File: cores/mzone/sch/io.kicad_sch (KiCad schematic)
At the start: 87 parts

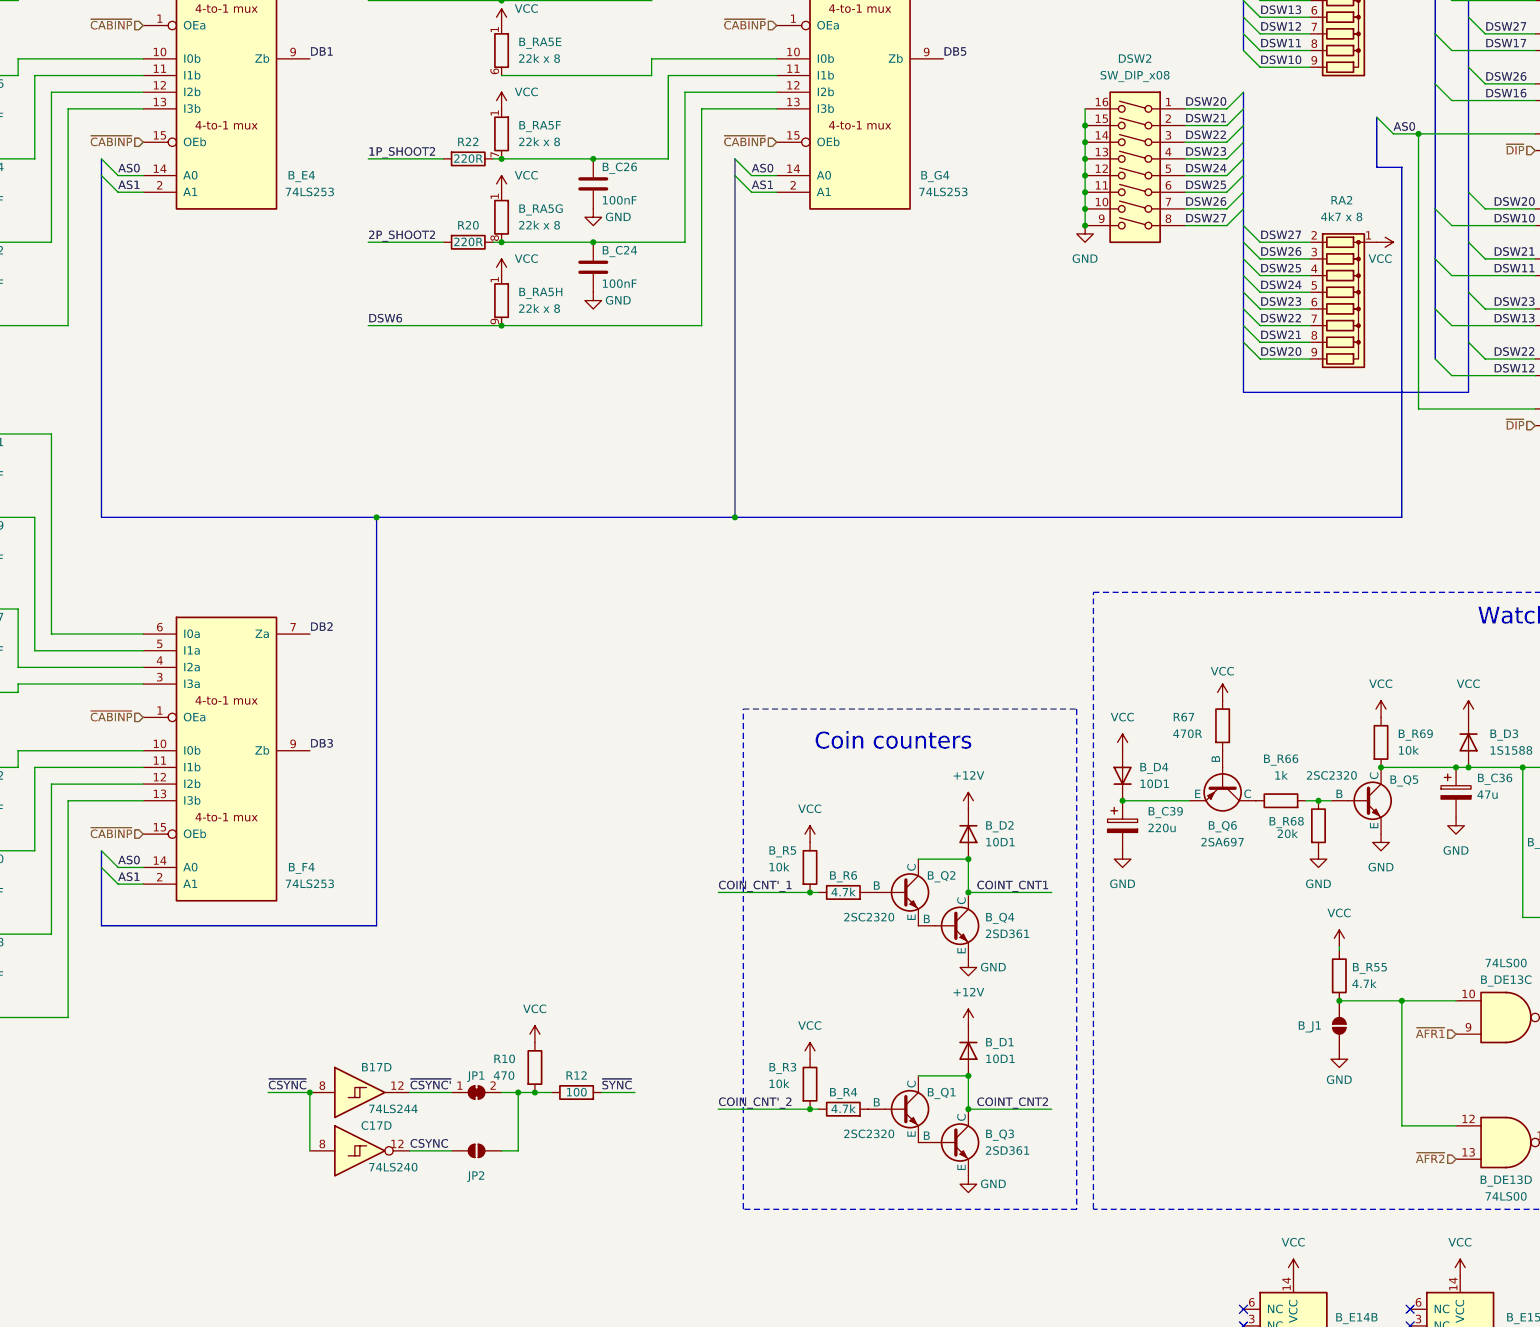
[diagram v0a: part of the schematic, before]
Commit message: mzone core
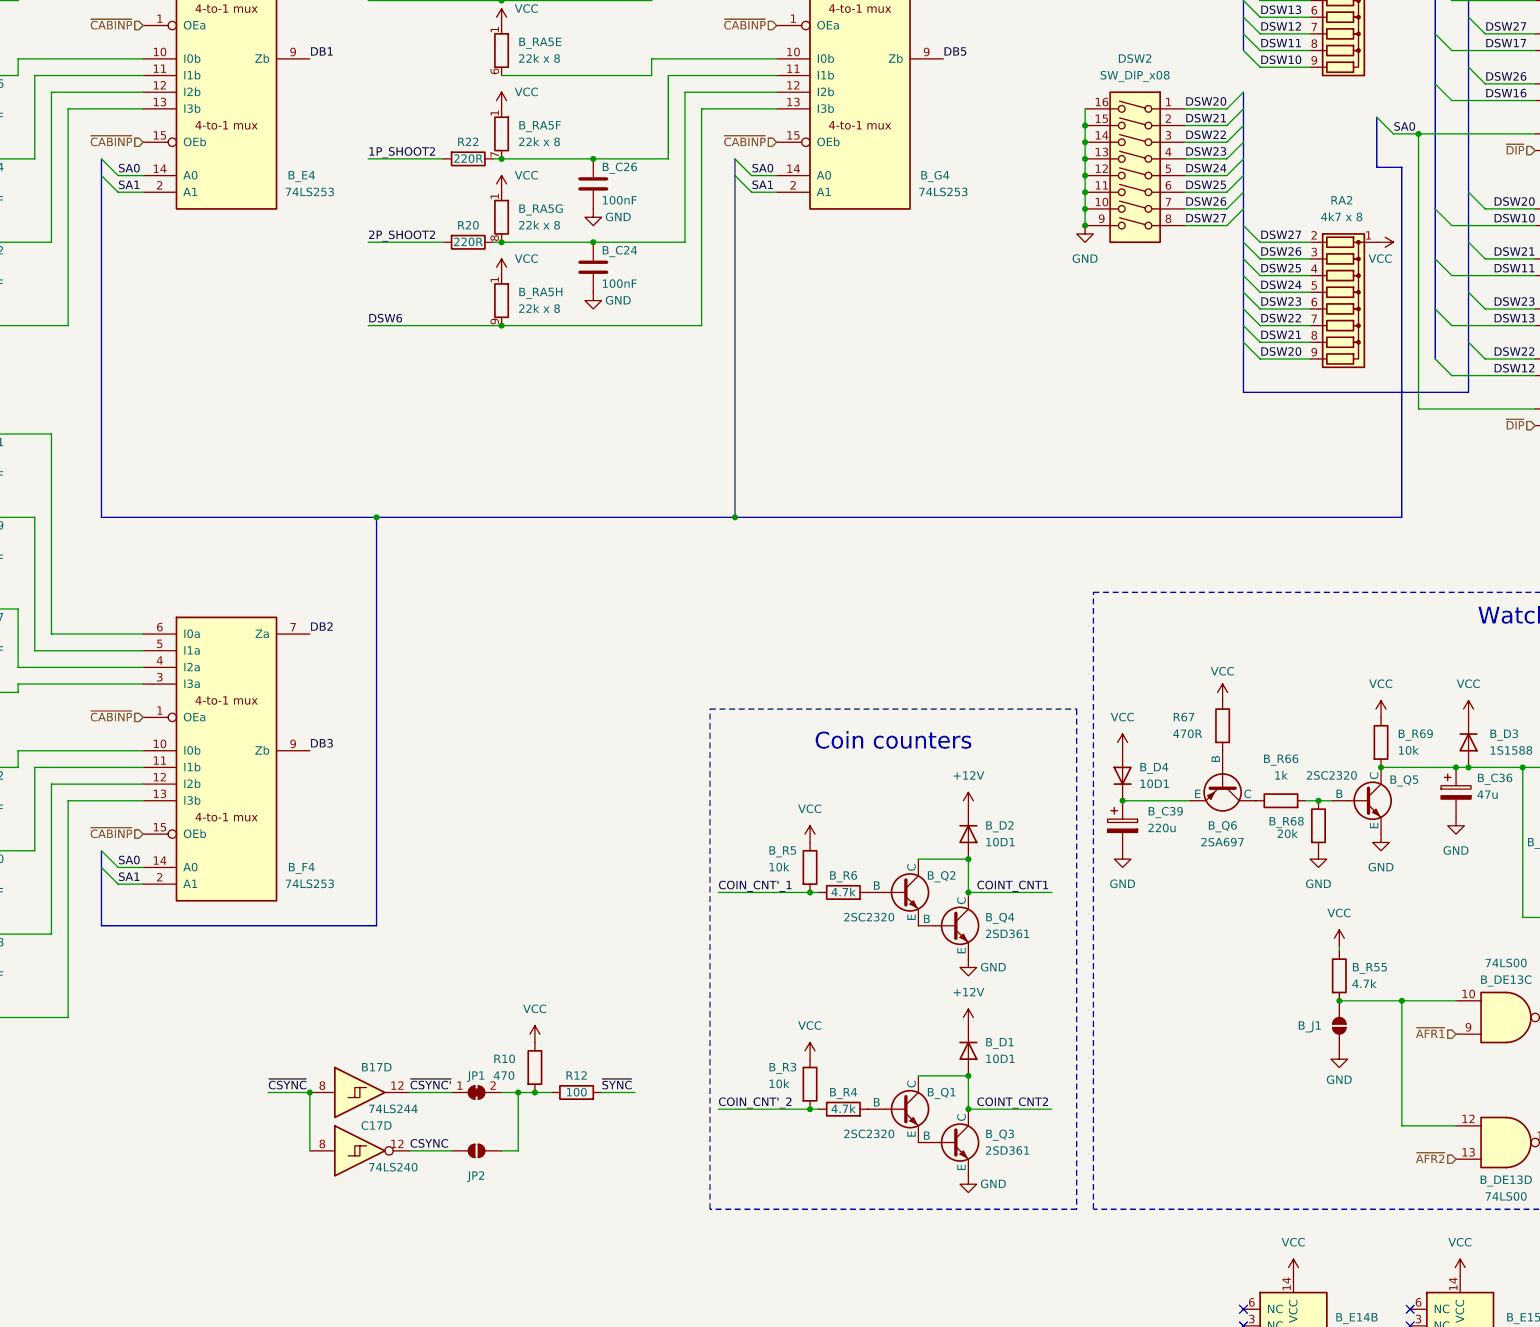
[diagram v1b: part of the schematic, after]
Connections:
- net AS0 renamed SA0
- net AS1 renamed SA1
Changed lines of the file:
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@@
 	)
 	(rectangle
-		(start 172.72 173.99)
+		(start 167.64 173.99)
 		(end 223.52 250.19)
 		(stroke
@@
 		)
 	)
-	(label "AS0"
+	(label "SA0"
 		(at 77.47 92.71 0)
 		(effects
@@
 		)
 	)
-	(label "AS0"
+	(label "SA0"
 		(at 271.78 86.36 0)
 		(effects
@@
 		)
 	)
-	(label "AS1"
+	(label "SA1"
 		(at 77.47 95.25 0)
 		(effects
@@
 		)
 	)
-	(label "AS1"
+	(label "SA1"
 		(at 173.99 95.25 0)
 		(effects
@@
 		)
 	)
-	(label "AS0"
+	(label "SA0"
 		(at 173.99 92.71 0)
 		(effects
@@
 		)
 	)
-	(label "AS0"
+	(label "SA0"
 		(at 77.47 198.12 0)
 		(effects
@@
 		)
 	)
-	(label "AS1"
+	(label "SA1"
 		(at 77.47 200.66 0)
 		(effects

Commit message: mzone core
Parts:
- added SW3: SW_DIP_x06, symbol Switch:SW_DIP_x06
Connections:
- net +12V: now also U?.B1 (+12V)
- net 1P_DOWN: now also U?.A11 (1P_DOWN)
- net 1P_RIGHT: now also U?.A8 (1P_RIGHT)
- net 1P_SHOOT1: now also U?.A7 (1P_BTN1)
- net 1P_SHOOT2: now also U?.A6 (1P_BTN2)
- net 1P_START: now also U?.A5 (1P_START)
- net 1P_UP: now also U?.A9 (1P_UP)
- net 2P_DOWN: now also U?.B9 (2P_DOWN)
- net 2P_LEFT: now also U?.A4 (2P_LEFT)
- net 2P_SHOOT1: now also U?.A3 (2P_BTN_1)
- net 2P_SHOOT2: now also U?.B3 (2P_BTN2)
- net 2P_START: now also U?.B5 (2P_START)
- net 2P_UP: now also U?.B6 (2P_UP)
- net COIN1: now also U?.A10 (COIN1)
- net DSW1: now also SW3.12
- net DSW2: now also SW3.11
- net DSW3: now also SW3.10
- net DSW4: now also SW3.9
- net DSW5: now also SW3.8
- net DSW6: now also SW3.7
- net GND: now also U?.A16 (GND), U?.A17 (GND), U?.B16 (GND), U?.B17 (GND), SW3.1, SW3.2, SW3.3, SW3.4, SW3.5, SW3.6
- net SERVICE: now also U?.B7 (SERVICE)
- net VCC: now also U?.A18 (+5V), U?.B18 (+5V)
- net ~{SYNC}: now also U?.B14 (VIDEO_SYNC)
- net GREEN: now reaches U?.A13 (VIDEO_GREEN)
- net RED: now reaches U?.A14 (VIDEO_RED)
- net BLUE: now reaches U?.B13 (VIDEO_BLUE)
- no-connect marks 7 -> 15
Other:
- moved on the sheet: B17D, B_E14A, B_E15A, B_E4, C17D, JP1, JP2, R10, R12

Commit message: mzone core
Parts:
- gave numbers to parts that had none: 1

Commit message: mzone core
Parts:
- renumbered R8 to B_R8, RA1 to B_RA1, RA2 to B_RA2

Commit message: mzone core
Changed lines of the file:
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@@
 	)
 	(junction
+		(at 349.25 110.49)
+		(diameter 0)
+		(color 0 0 0 0)
+	)
+	(junction
 		(at 39.37 220.98)
 		(diameter 0)
@@
 	)
 	(junction
+		(at 349.25 113.03)
+		(diameter 0)
+		(color 0 0 0 0)
+	)
+	(junction
 		(at 378.46 135.89)
 		(diameter 0)
@@
 	)
 	(symbol
+		(lib_id "power:PWR_FLAG")
+		(at 349.25 110.49 90)
+		(unit 1)
+		(exclude_from_sim no)
+		(in_bom yes)
+		(on_board yes)
+		(dnp no)
+		(property "Reference" "#FLG02"
+			(at 347.345 110.49 0)
+			(effects
+				(font
+					(size 1.27 1.27)
+				)
+				(hide yes)
+			)
+		)
+		(property "Value" "PWR_FLAG"
+			(at 341.63 110.49 90)
+			(effects
+				(font
+					(size 1.27 1.27)
+				)
+			)
+		)
+		(property "Footprint" ""
+			(at 349.25 110.49 0)
+			(effects
+				(font
+					(size 1.27 1.27)
+				)
+				(hide yes)
+			)
+		)
+		(property "Datasheet" "~"
+			(at 349.25 110.49 0)
+			(effects
+				(font
+					(size 1.27 1.27)
+				)
+				(hide yes)
+			)
+		)
+		(property "Description" "Special symbol for telling ERC where power comes from"
+			(at 349.25 110.49 0)
+			(effects
+				(font
+					(size 1.27 1.27)
+				)
+				(hide yes)
+			)
+		)
+		(pin "1"
+		)
+		(instances
+			(project "megazone"
+				(path "/b3e039a8-74b0-4cb4-b612-5df1f0b42747/fc0cdb6a-9224-4695-8376-e66e14e5242d"
+					(reference "#FLG02")
+					(unit 1)
+				)
+			)
+		)
+	)
+	(symbol
 		(lib_id "Device:R_Network08_Split")
 		(at 39.37 111.76 0)
@@
 			)
 		)
-		(property "Description" ""
+		(property "Description" "Quad And2"
 			(at 360.68 185.42 0)
 			(effects
@@
 			)
 		)
-		(property "Description" ""
+		(property "Description" "quad 2-input NAND gate"
 			(at 288.925 220.98 0)
 			(effects
@@
 			)
 		)
-		(property "Description" ""
+		(property "Description" "Quad And2"
 			(at 375.92 204.47 0)
 			(effects
@@
 			)
 		)
-		(property "Description" ""
+		(property "Description" "quad 2-input NAND gate"
 			(at 288.925 240.03 0)
 			(effects
@@
 	)
 	(symbol
+		(lib_id "power:PWR_FLAG")
+		(at 349.25 113.03 180)
+		(unit 1)
+		(exclude_from_sim no)
+		(in_bom yes)
+		(on_board yes)
+		(dnp no)
+		(property "Reference" "#FLG01"
+			(at 349.25 114.935 0)
+			(effects
+				(font
+					(size 1.27 1.27)
+				)
+				(hide yes)
+			)
+		)
+		(property "Value" "PWR_FLAG"
+			(at 349.25 116.84 0)
+			(effects
+				(font
+					(size 1.27 1.27)
+				)
+			)
+		)
+		(property "Footprint" ""
+			(at 349.25 113.03 0)
+			(effects
+				(font
+					(size 1.27 1.27)
+				)
+				(hide yes)
+			)
+		)
+		(property "Datasheet" "~"
+			(at 349.25 113.03 0)
+			(effects
+				(font
+					(size 1.27 1.27)
+				)
+				(hide yes)
+			)
+		)
+		(property "Description" "Special symbol for telling ERC where power comes from"
+			(at 349.25 113.03 0)
+			(effects
+				(font
+					(size 1.27 1.27)
+				)
+				(hide yes)
+			)
+		)
+		(pin "1"
+		)
+		(instances
+			(project ""
+				(path "/b3e039a8-74b0-4cb4-b612-5df1f0b42747/fc0cdb6a-9224-4695-8376-e66e14e5242d"
+					(reference "#FLG01")
+					(unit 1)
+				)
+			)
+		)
+	)
+	(symbol
 		(lib_id "power:GND")
 		(at 53.34 166.37 0)
@@
 			)
 		)
-		(property "Description" ""
+		(property "Description" "quad 2-input NOR gate"
 			(at 343.535 223.52 0)
 			(effects
